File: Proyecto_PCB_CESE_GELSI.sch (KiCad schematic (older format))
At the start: 19 parts, among them IC1 SC2272L4, IC2 ASM1117-33, IC3 SN74LVC1G125DCKR, IC4 H5V3G

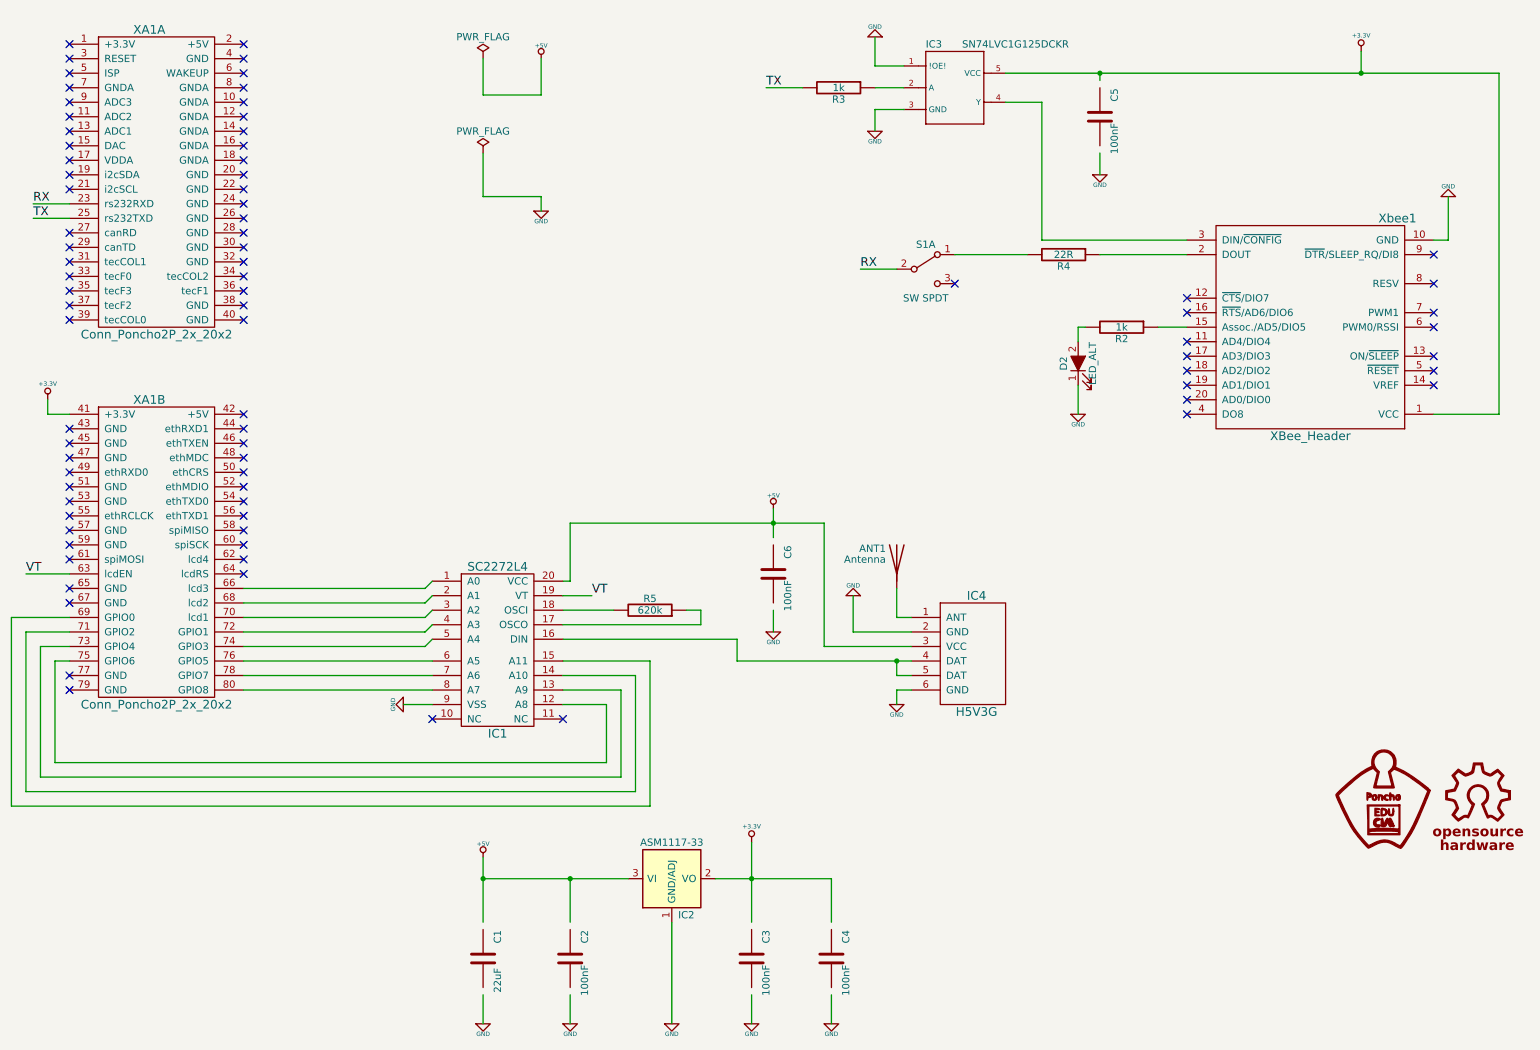
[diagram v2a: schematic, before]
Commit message: Update en proyecto
Correciones realizadas luego de que fueran marcadas por el revisor. Además se incorporó una única carpeta de librearías, que era en lo que venía trabajándose para llegar a esto antes de la primer entrega.
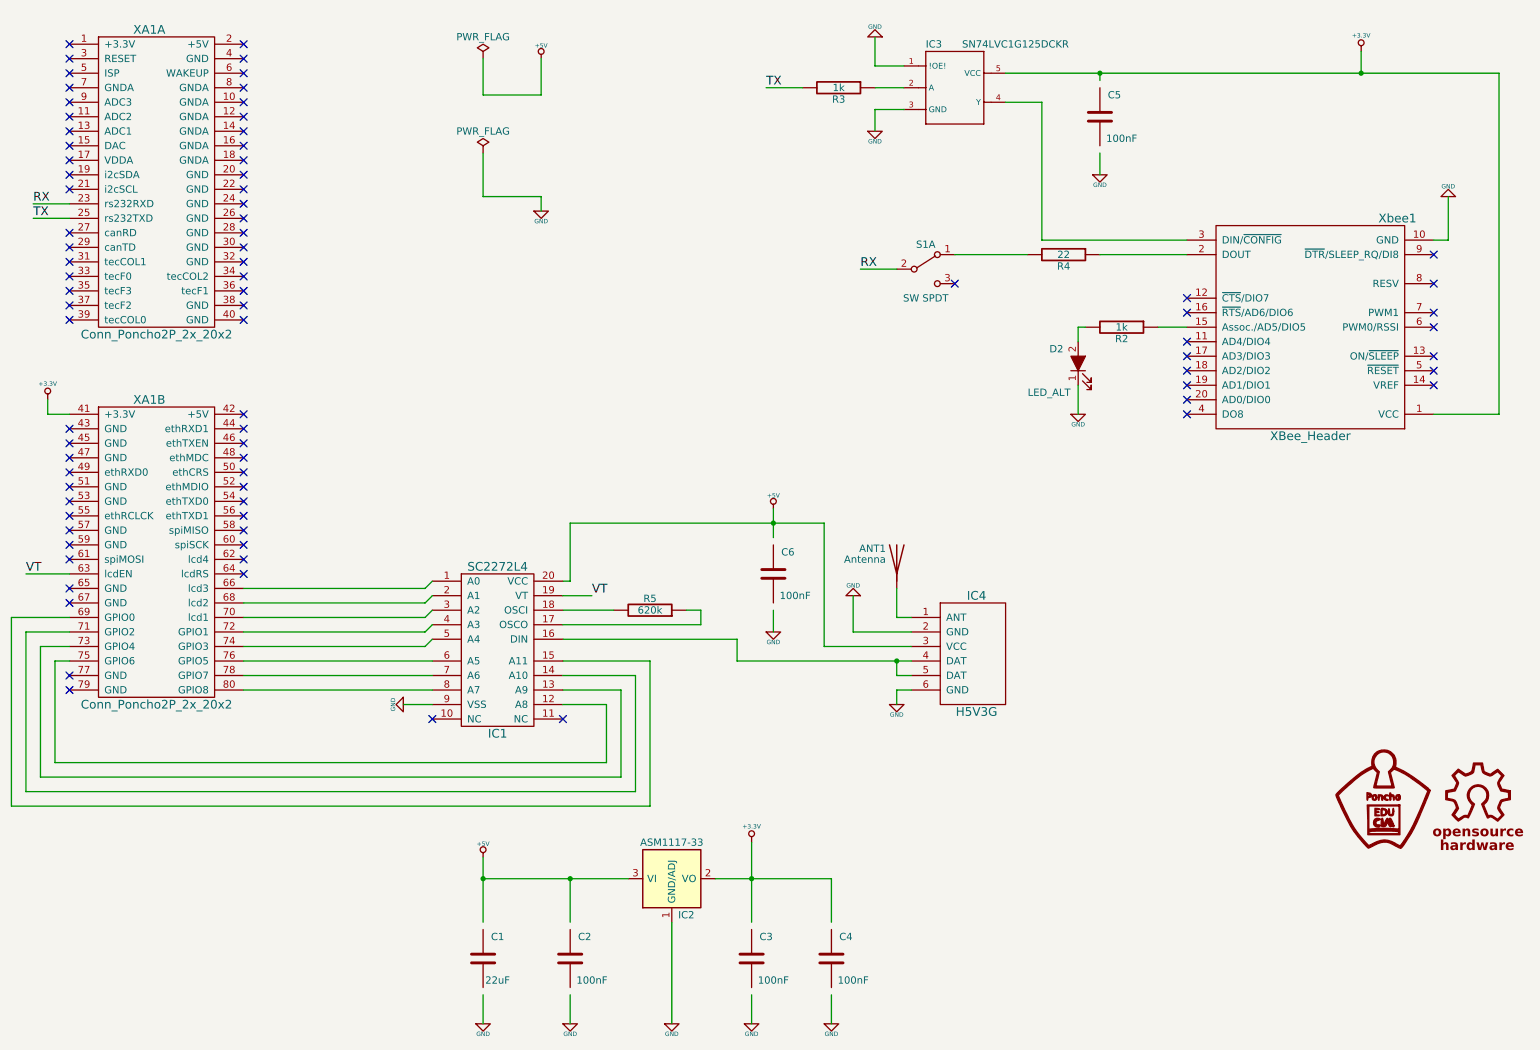
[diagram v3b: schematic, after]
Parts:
- R4: value 22R -> 22
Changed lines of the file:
@@
 U 1 1 5920A1DC
 P 3950 7100
-F 0 "C1" V 4050 7250 50  0000 C CNN
-F 1 "22uF" V 4050 6950 50  0000 C CNN
+F 0 "C1" H 4050 7250 50  0000 C CNN
+F 1 "22uF" H 4050 6950 50  0000 C CNN
 F 2 "projectHuellas:C_0603_HandSoldering" H 3950 7100 50  0001 C CNN
 F 3 "" H 3950 7100 50  0001 C CNN
@@
 U 1 1 5920A243
 P 4550 7100
-F 0 "C2" V 4650 7250 50  0000 C CNN
-F 1 "100nF" V 4650 6950 50  0000 C CNN
+F 0 "C2" H 4650 7250 50  0000 C CNN
+F 1 "100nF" H 4700 6950 50  0000 C CNN
 F 2 "projectHuellas:C_0603_HandSoldering" H 4550 7100 50  0001 C CNN
 F 3 "" H 4550 7100 50  0001 C CNN
@@
 U 1 1 5920A2D5
 P 5800 7100
-F 0 "C3" V 5900 7250 50  0000 C CNN
-F 1 "100nF" V 5900 6950 50  0000 C CNN
+F 0 "C3" H 5900 7250 50  0000 C CNN
+F 1 "100nF" H 5950 6950 50  0000 C CNN
 F 2 "projectHuellas:C_0603_HandSoldering" H 5800 7100 50  0001 C CNN
 F 3 "" H 5800 7100 50  0001 C CNN
@@
 U 1 1 5920A33B
 P 6350 7100
-F 0 "C4" V 6450 7250 50  0000 C CNN
-F 1 "100nF" V 6450 6950 50  0000 C CNN
+F 0 "C4" H 6450 7250 50  0000 C CNN
+F 1 "100nF" H 6500 6950 50  0000 C CNN
 F 2 "projectHuellas:C_0603_HandSoldering" H 6350 7100 50  0001 C CNN
 F 3 "" H 6350 7100 50  0001 C CNN
@@
 U 1 1 5920B0A6
 P 5950 4450
-F 0 "C6" V 6050 4600 50  0000 C CNN
-F 1 "100nF" V 6050 4300 50  0000 C CNN
+F 0 "C6" H 6050 4600 50  0000 C CNN
+F 1 "100nF" H 6100 4300 50  0000 C CNN
 F 2 "projectHuellas:C_0603_HandSoldering" H 5950 4450 50  0001 C CNN
 F 3 "" H 5950 4450 50  0001 C CNN
@@
 F 1 "SN74LVC1G125DCKR" H 7250 1400 50  0000 L CNN
 F 2 "projectHuellas:SC-70-5" H 7200 1100 50  0001 L CNN
-F 3 "Texas Instruments" H 7200 1100 50  0001 L CNN
+F 3 "" H 7200 1100 50  0001 L CNN
 F 4 "Texas Instruments" H 7200 1100 60  0001 C CNN "Manf"
 F 5 "SN74LVC1G125DCKR" H 7200 1100 60  0001 C CNN "Manf#"
@@
 U 1 1 5920BF30
 P 8200 1300
-F 0 "C5" V 8300 1450 50  0000 C CNN
-F 1 "100nF" V 8300 1150 50  0000 C CNN
+F 0 "C5" H 8300 1450 50  0000 C CNN
+F 1 "100nF" H 8350 1150 50  0000 C CNN
 F 2 "projectHuellas:C_0603_HandSoldering" H 8200 1300 50  0001 C CNN
 F 3 "" H 8200 1300 50  0001 C CNN
@@
 P 7950 2250
 F 0 "R4" V 8030 2250 50  0000 C CNN
-F 1 "22R" V 7950 2250 50  0000 C CNN
+F 1 "22" V 7950 2250 50  0000 C CNN
 F 2 "projectHuellas:R_1206_HandSoldering" H 7950 2250 50  0001 C CNN
 F 3 "" H 7950 2250 50  0001 C CNN
@@
 U 1 1 5920DE9D
 P 8050 3000
-F 0 "D2" H 8050 3100 50  0000 C CNN
-F 1 "LED_ALT" H 8050 2900 50  0000 C CNN
+F 0 "D2" V 8150 3150 50  0000 C CNN
+F 1 "LED_ALT" V 7850 3200 50  0000 C CNN
 F 2 "projectHuellas:D_0805" H 8050 3000 50  0001 C CNN
 F 3 "" H 8050 3000 50  0001 C CNN

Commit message: Update en el proyecto (Correcciones parciales de 1ra fecha)
Se corrigieron algunas cosas marcadas en la 1ra fecha.
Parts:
- IC1: Manf (none) -> http://www.ebay.es/itm/2-x-SC2272-L4-Remote-Control-Decoder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; Price (none) -> 1.50
- IC4: Manf (none) -> http://162.250.126.230/item/Free-Shipping-1pc-ASK-superhete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
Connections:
- net labels removed: RX, TX, VT
- wire segments 103 -> 108
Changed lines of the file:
@@
 Comment1 "https://github.com/ciaa/Ponchos/tree/master/modelos/doc"
 Comment2 "Autores y Licencia del template (Diego Brengi - UNLaM)"
-Comment3 "Autor del poncho (Fabrizio Gelsi). Ver directorio \"doc\""
-Comment4 "CÓDIGO PONCHO:"
+Comment3 "Revisor: Alan Toris. Ver directorio \"doc\""
+Comment4 "Autor del poncho (Fabrizio Gelsi). "
 $EndDescr
 $Comp
@@
 F 2 "projectHuellas:H5V3G" H 7350 5000 60  0001 C CNN
 F 3 "" H 7350 5000 60  0001 C CNN
+F 4 "http://162.250.126.230/item/Free-Shipping-1pc-ASK-superheterodyne-315M-miniature-receiver-5V-low-power-wireless-module-H5V3G-PCB-bare/1419753175.html" H 7350 5000 60  0001 C CNN "Manf"
 	1    7350 5000
 	1    0    0    -1
@@
 L +3.3V #PWR016
 U 1 1 5920BEA5
-P 10000 850
-F 0 "#PWR016" H 10000 810 30  0001 C CNN
-F 1 "+3.3V" H 10000 960 30  0000 C CNN
-F 2 "" H 10000 850 60  0001 C CNN
-F 3 "" H 10000 850 60  0001 C CNN
-	1    10000 850
+P 8200 850
+F 0 "#PWR016" H 8200 810 30  0001 C CNN
+F 1 "+3.3V" H 8200 960 30  0000 C CNN
+F 2 "" H 8200 850 60  0001 C CNN
+F 3 "" H 8200 850 60  0001 C CNN
+	1    8200 850
 	1    0    0    -1
 $EndComp
@@
 F 2 "projectHuellas:SSOP-20_5.3x7.2mm_Pitch0.65mm" H 4050 4950 60  0001 C CNN
 F 3 "" H 4050 4950 60  0001 C CNN
+F 4 "http://www.ebay.es/itm/2-x-SC2272-L4-Remote-Control-Decoder-SC2272-PT2272-L4-/300530137263" H 4050 4950 60  0001 C CNN "Manf"
+F 5 "1.50" H 4050 4950 60  0001 C CNN "Price"
 	1    4050 4950
 	1    0    0    -1
@@
 	1    0    0    -1
 $EndComp
-Text Label 6550 2350 0    60   ~ 0
-RX
-Text Label 5900 1100 0    60   ~ 0
-TX
 $Comp
 L Conn_Poncho2P_2x_20x2 XA1
@@
 	1    0    0    -1
 $EndComp
-Text Label 850  2000 0    60   ~ 0
-TX
-Text Label 850  1900 0    60   ~ 0
-RX
 NoConn ~ 3600 5450
 NoConn ~ 4500 5450
@@
 	10600 2150 10600 1850
 Wire Wire Line
-	10500 3350 10950 3350
-Wire Wire Line
-	10950 3350 10950 1000
-Wire Wire Line
-	10950 1000 7550 1000
-Wire Wire Line
-	8200 1050 8200 1000
-Connection ~ 8200 1000
-Wire Wire Line
-	10000 850  10000 1000
-Connection ~ 10000 1000
-Wire Wire Line
 	8200 1550 8200 1700
 Wire Wire Line
@@
 Wire Wire Line
 	6300 4950 6300 4100
-Wire Wire Line
-	6300 4100 4550 4100
-Wire Wire Line
-	4550 4100 4550 4500
 Wire Wire Line
 	4550 4500 4500 4500
@@
 	5100 5050 4500 5050
 Wire Wire Line
-	6550 2350 6800 2350
-Wire Wire Line
-	5900 1100 6150 1100
-Wire Wire Line
-	850  1900 1100 1900
+	6300 2350 6800 2350
+Wire Wire Line
+	5500 1100 6150 1100
+Wire Wire Line
+	750  1900 1100 1900
 Wire Wire Line
 	850  2000 1100 2000
@@
 NoConn ~ 8800 3350
 Wire Wire Line
-	4500 4600 4700 4600
-Text Label 4700 4600 0    60   ~ 0
-VT
+	4500 4600 4900 4600
 Wire Wire Line
 	1100 4450 800  4450
-Text Label 800  4450 0    60   ~ 0
-VT
 NoConn ~ 1100 2700
 NoConn ~ 1100 2600
@@
 NoConn ~ 2300 900
 NoConn ~ 2300 800
-NoConn ~ 2300 3350
 NoConn ~ 2300 3450
 NoConn ~ 2300 3550
@@
 	3950 1850 3950 1550
 Wire Wire Line
-	3950 900  3950 1150
-Wire Wire Line
-	3950 1150 4350 1150
-Wire Wire Line
-	4350 1150 4350 900
+	850  2000 850  2900
+Wire Wire Line
+	850  2900 5500 2900
+Wire Wire Line
+	5500 2900 5500 1100
+Wire Wire Line
+	750  1900 750  3000
+Wire Wire Line
+	750  3000 6300 3000
+Wire Wire Line
+	6300 3000 6300 2350
+Wire Wire Line
+	6300 4100 5950 4100
 $Comp
 L +5V #PWR021
-U 1 1 59297E0B
-P 4350 900
-F 0 "#PWR021" H 4350 990 20  0001 C CNN
-F 1 "+5V" H 4350 990 30  0000 C CNN
-F 2 "" H 4350 900 60  0000 C CNN
-F 3 "" H 4350 900 60  0000 C CNN
-	1    4350 900
-	1    0    0    -1
-$EndComp
-$Comp
-L PWR_FLAG #FLG022
-U 1 1 59297BC7
-P 3950 900
-F 0 "#FLG022" H 3950 975 50  0001 C CNN
-F 1 "PWR_FLAG" H 3950 1050 50  0000 C CNN
-F 2 "" H 3950 900 50  0001 C CNN
-F 3 "" H 3950 900 50  0001 C CNN
-	1    3950 900
-	1    0    0    -1
-$EndComp
-$Comp
-L +3.3V #PWR023
-U 1 1 592FECE1
-P 950 3250
-F 0 "#PWR023" H 950 3210 30  0001 C CNN
-F 1 "+3.3V" H 950 3360 30  0000 C CNN
-F 2 "" H 950 3250 60  0000 C CNN
-F 3 "" H 950 3250 60  0000 C CNN
-	1    950  3250
-	1    0    0    -1
-$EndComp
-Wire Wire Line
-	950  3250 950  3350
-Wire Wire Line
-	950  3350 1100 3350
+U 1 1 59619575
+P 4550 4400
+F 0 "#PWR021" H 4550 4490 20  0001 C CNN
+F 1 "+5V" H 4550 4490 30  0000 C CNN
+F 2 "" H 4550 4400 60  0001 C CNN
+F 3 "" H 4550 4400 60  0001 C CNN
+	1    4550 4400
+	1    0    0    -1
+$EndComp
+Wire Wire Line
+	4550 4500 4550 4400
+Wire Wire Line
+	8200 1050 8200 850
+Wire Wire Line
+	7550 1000 8200 1000
+Connection ~ 8200 1000
+$Comp
+L +3.3V #PWR022
+U 1 1 596199FD
+P 10750 3250
+F 0 "#PWR022" H 10750 3210 30  0001 C CNN
+F 1 "+3.3V" H 10750 3360 30  0000 C CNN
+F 2 "" H 10750 3250 60  0001 C CNN
+F 3 "" H 10750 3250 60  0001 C CNN
+	1    10750 3250
+	1    0    0    -1
+$EndComp
+Wire Wire Line
+	10500 3350 10750 3350
+Wire Wire Line
+	10750 3350 10750 3250
+Wire Wire Line
+	800  4450 800  3100
+Wire Wire Line
+	800  3100 4900 3100
+Wire Wire Line
+	4900 3100 4900 4600
+NoConn ~ 1100 3350
+$Comp
+L +5V #PWR023
+U 1 1 5961AEFB
+P 2400 3300
+F 0 "#PWR023" H 2400 3390 20  0001 C CNN
+F 1 "+5V" H 2400 3390 30  0000 C CNN
+F 2 "" H 2400 3300 60  0000 C CNN
+F 3 "" H 2400 3300 60  0000 C CNN
+	1    2400 3300
+	1    0    0    -1
+$EndComp
+Wire Wire Line
+	2300 3350 2400 3350
+Wire Wire Line
+	2400 3350 2400 3300
 $EndSCHEMATC

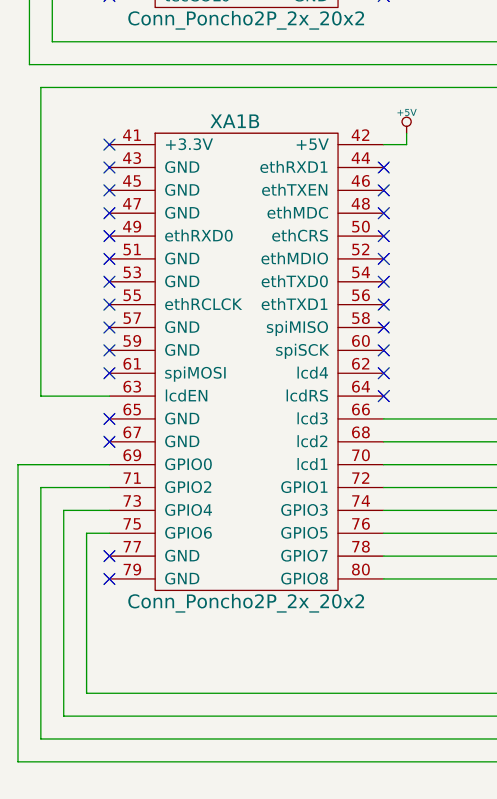
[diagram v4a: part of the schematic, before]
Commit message: Update en proyecto
Se resolvieron algunos problemas referidos al PCB, a fin de corregir los errores marcados durante la primer entrega. Por problemas con el IDE KICAD, se dejaron algunos para la tercer entrega.
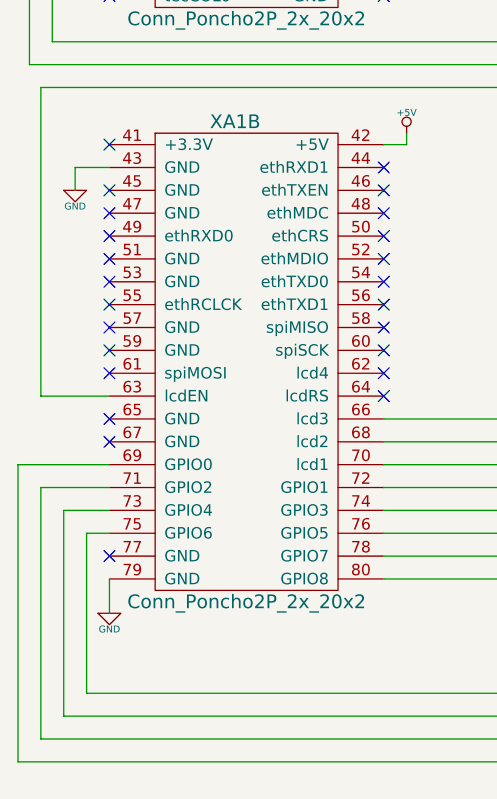
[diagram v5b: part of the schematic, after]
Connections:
- wire segments 108 -> 111
- no-connect marks 82 -> 80
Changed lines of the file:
@@
 Comment1 "https://github.com/ciaa/Ponchos/tree/master/modelos/doc"
 Comment2 "Autores y Licencia del template (Diego Brengi - UNLaM)"
-Comment3 "Revisor: Alan Toris. Ver directorio \"doc\""
-Comment4 "Autor del poncho (Fabrizio Gelsi). "
+Comment3 "Autor del poncho (Fabrizio Gelsi). Revisor: Alan Toris. Ver directorio \"doc\""
+Comment4 "Asignatura: Curso de diseño de circuitos impresos"
 $EndDescr
 $Comp
@@
 NoConn ~ 4500 5450
 NoConn ~ 1100 5150
-NoConn ~ 1100 5250
 Wire Wire Line
 	3950 6550 4950 6550
@@
 NoConn ~ 1100 3650
 NoConn ~ 1100 3550
-NoConn ~ 1100 3450
 Wire Wire Line
 	5800 6300 5800 6850
@@
 Wire Wire Line
 	2400 3350 2400 3300
+$Comp
+L GND #PWR024
+U 1 1 596A4BCF
+P 950 3550
+F 0 "#PWR024" H 950 3550 30  0001 C CNN
+F 1 "GND" H 950 3480 30  0000 C CNN
+F 2 "" H 950 3550 60  0001 C CNN
+F 3 "" H 950 3550 60  0001 C CNN
+	1    950  3550
+	1    0    0    -1
+$EndComp
+Wire Wire Line
+	1100 3450 950  3450
+Wire Wire Line
+	950  3450 950  3550
+$Comp
+L GND #PWR025
+U 1 1 596A4DA5
+P 1100 5400
+F 0 "#PWR025" H 1100 5400 30  0001 C CNN
+F 1 "GND" H 1100 5330 30  0000 C CNN
+F 2 "" H 1100 5400 60  0001 C CNN
+F 3 "" H 1100 5400 60  0001 C CNN
+	1    1100 5400
+	1    0    0    -1
+$EndComp
+Wire Wire Line
+	1100 5250 1100 5400
 $EndSCHEMATC
